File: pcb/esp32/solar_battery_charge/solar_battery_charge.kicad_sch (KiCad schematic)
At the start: 15 parts, among them J1 USB_A, J2 capacitor2, J3 Conn_01x02_Female, J4 Screw_Terminal_01x02, J5 Conn_01x02_Female, J6 Conn_01x02_Female, J7 capacitor1, U1 LM7805_TO220, U2 LM1117-5.0, U3 TP4056_complete_module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

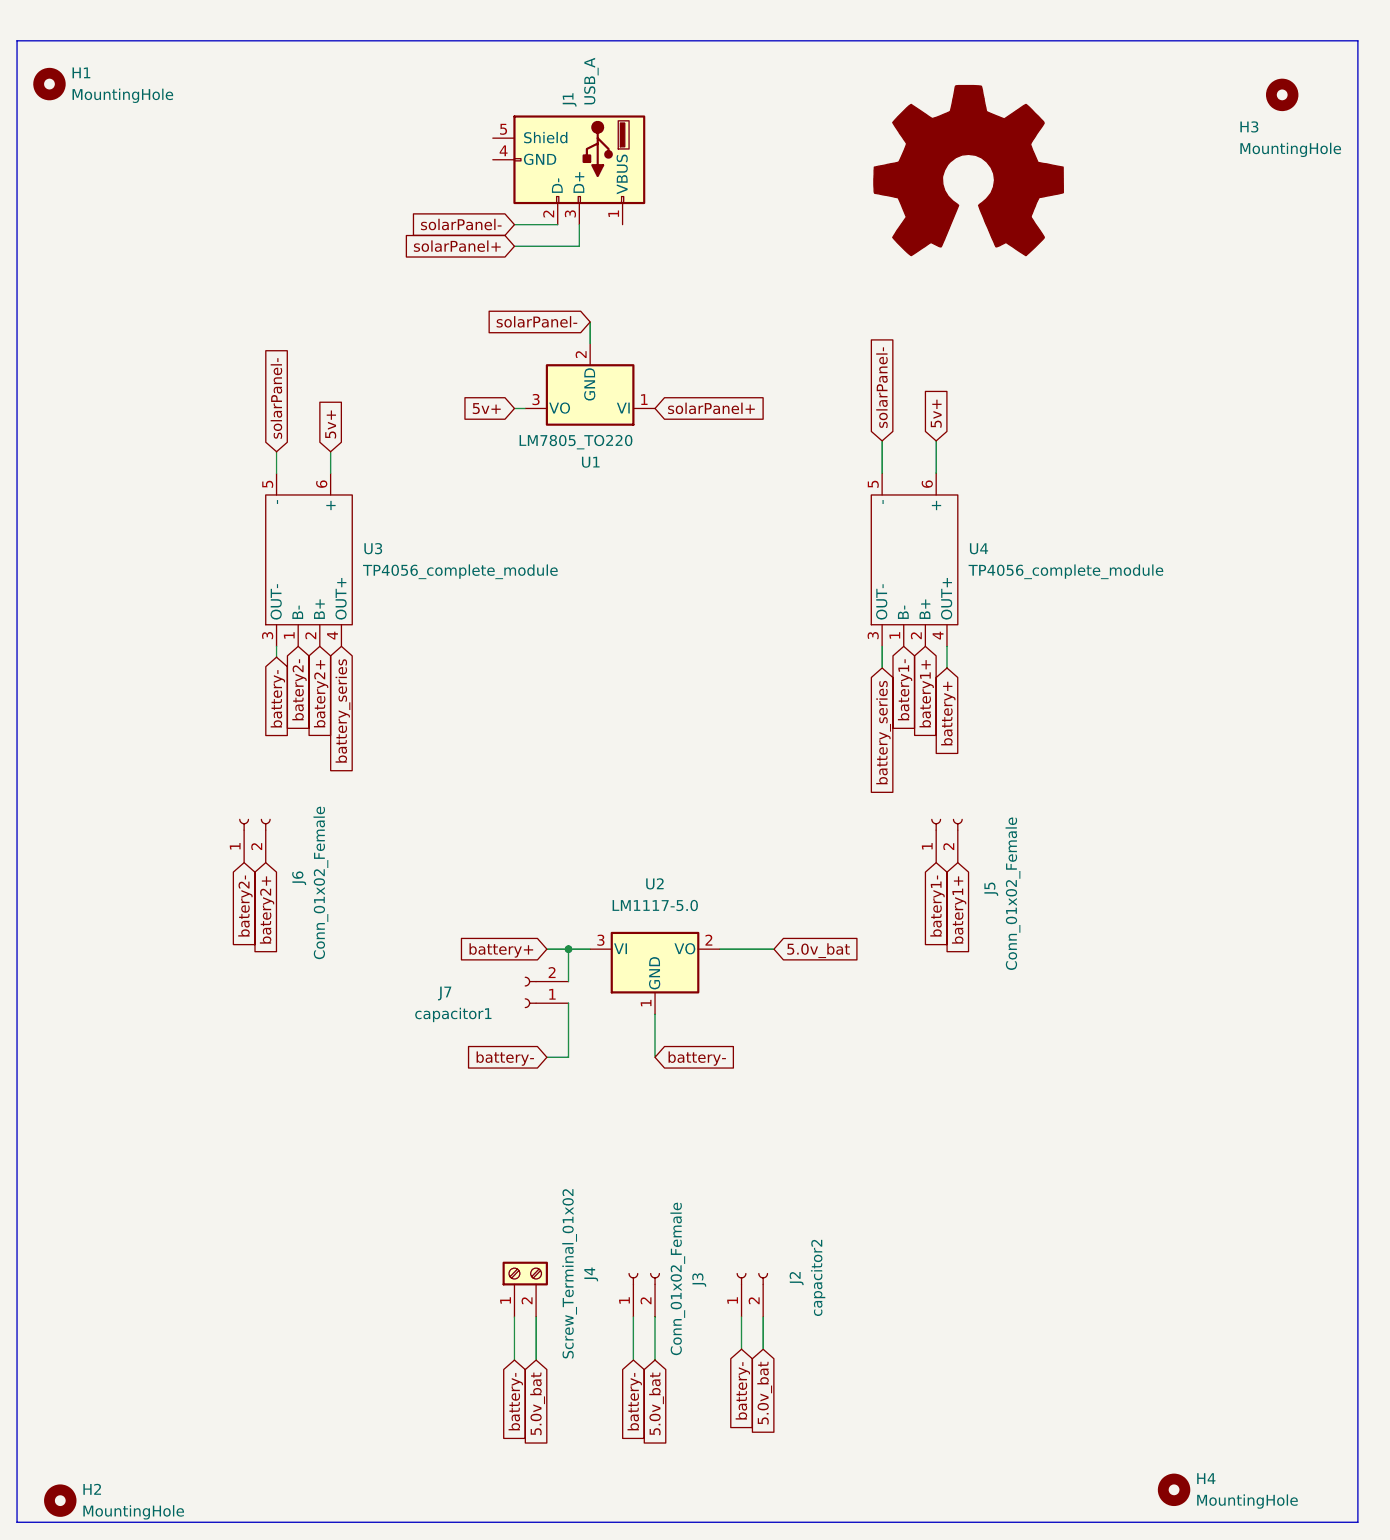
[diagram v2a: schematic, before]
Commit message: added 2 pairs of male pins to measure solar panel voltage and battery voltage
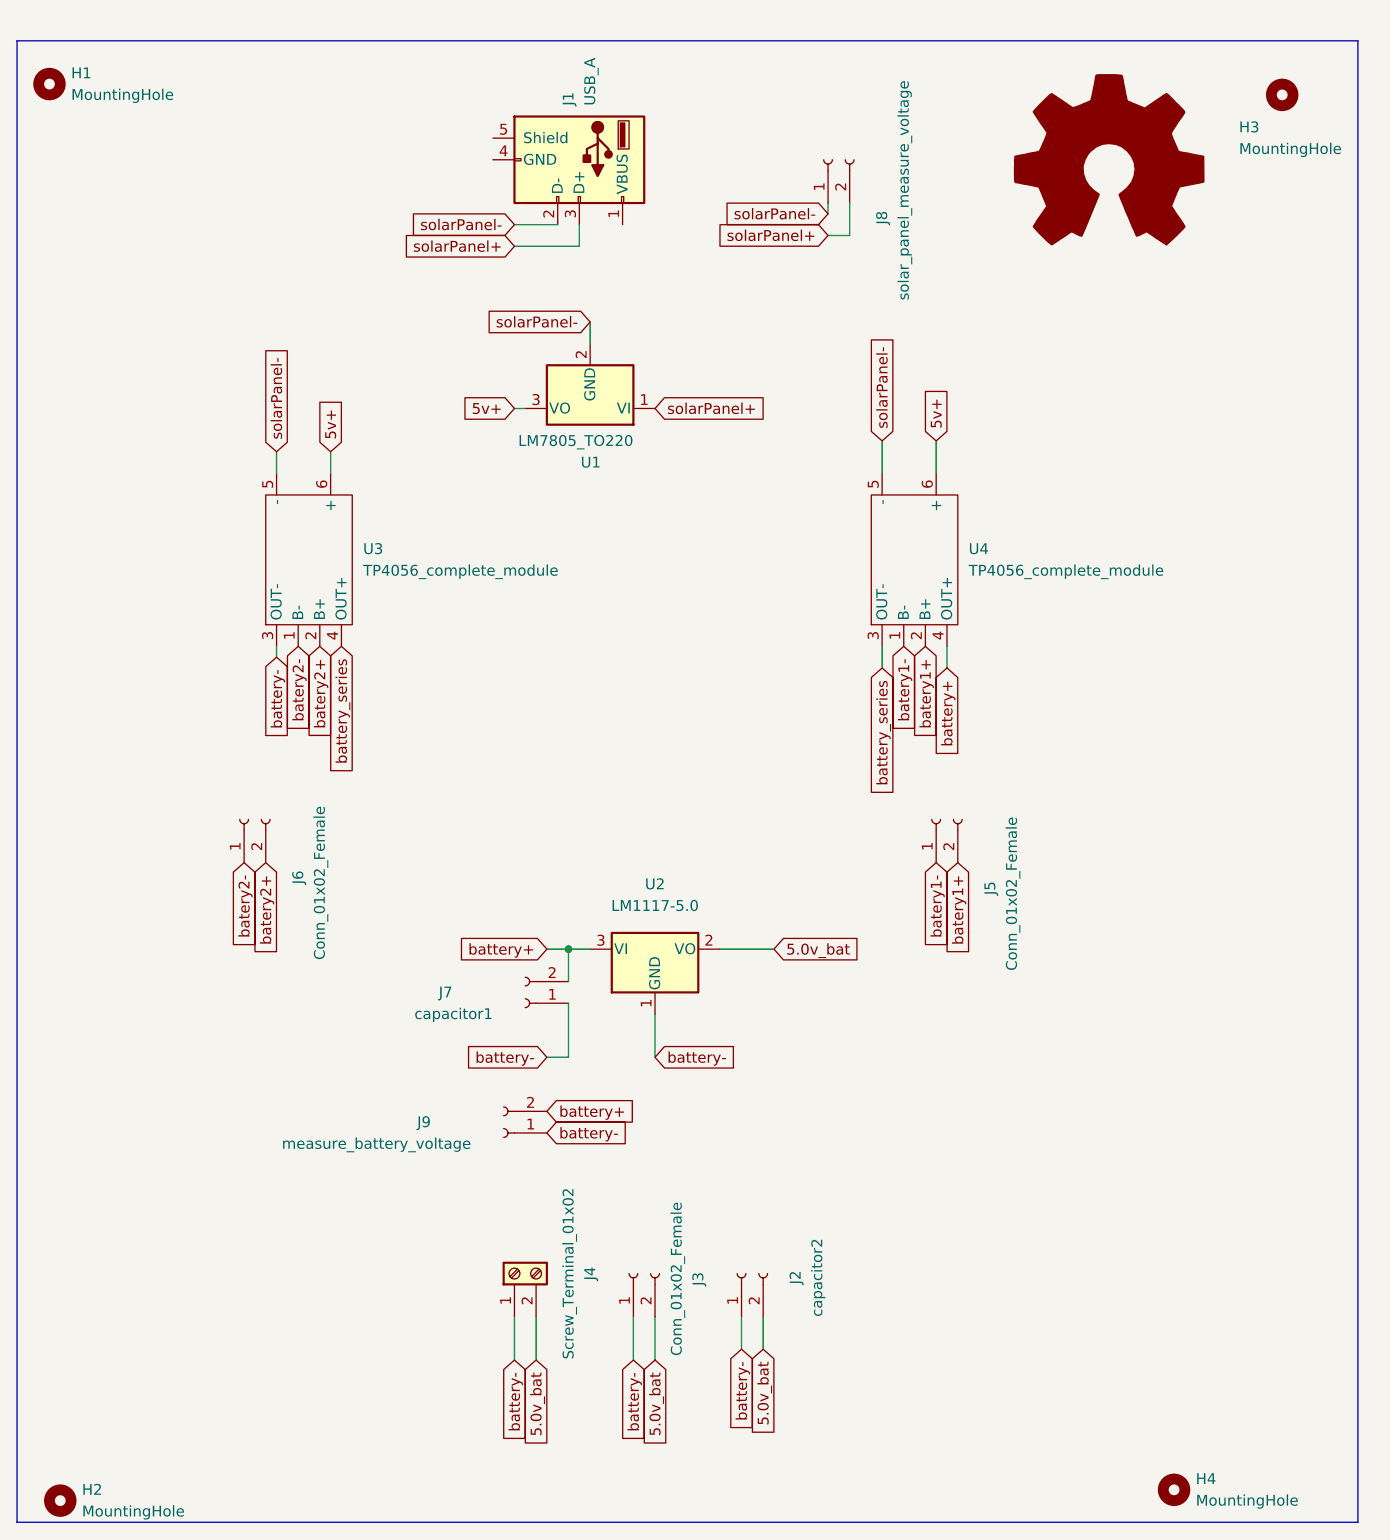
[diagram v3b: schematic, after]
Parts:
- added J8: solar_panel_measure_voltage, smart_sensor:Connector_Molex_Molex_SL_171971-0004_1x02_P2.54mm_Vertical_squares, symbol Connector:Conn_01x02_Female
- added J9: measure_battery_voltage, smart_sensor:Connector_Molex_Molex_SL_171971-0004_1x02_P2.54mm_Vertical_squares, symbol Connector:Conn_01x02_Female
- U2: footprint (none) -> Package_TO_SOT_SMD:SOT-223-3_TabPin2
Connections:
- net battery+: now also J9.2 (Pin_2)
- net battery-: now also J9.1 (Pin_1)
- net solarPanel+: now also J8.2 (Pin_2)
- net solarPanel-: now also J8.1 (Pin_1)
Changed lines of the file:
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@@
   (junction (at 80.01 121.92) (diameter 0) (color 0 0 0 0)
   )
+  (wire (pts (xy 113.03 34.29) (xy 113.03 38.1))
+    (stroke (width 0) (type default) (color 0 0 0 0))
+  )
   (wire (pts (xy 124.46 88.9) (xy 124.46 86.36))
     (stroke (width 0) (type default) (color 0 0 0 0))
@@
     (stroke (width 0) (type default) (color 0 0 0 0))
   )
+  (wire (pts (xy 113.03 38.1) (xy 110.49 38.1))
+    (stroke (width 0) (type default) (color 0 0 0 0))
+  )
   (wire (pts (xy 80.01 128.27) (xy 80.01 134.62))
     (stroke (width 0) (type default) (color 0 0 0 0))
@@
     (stroke (width 0) (type default) (color 0 0 0 0))
   )
+  (wire (pts (xy 110.49 34.29) (xy 110.49 35.56))
+    (stroke (width 0) (type default) (color 0 0 0 0))
+  )
   (wire (pts (xy 90.17 165.1) (xy 90.17 170.18))
     (stroke (width 0) (type default) (color 0 0 0 0))
@@
     )
   )
+  (global_label "solarPanel+" (shape input) (at 110.49 38.1 180) (fields_autoplaced)
+    (effects (font (size 1.27 1.27)) (justify right))
+    (property "Intersheet References" "${INTERSHEET_REFS}" (id 0) (at 96.405 38.1794 0)
+      (effects (font (size 1.27 1.27)) (justify right) hide)
+    )
+  )
   (global_label "battery+" (shape input) (at 124.46 88.9 270) (fields_autoplaced)
     (effects (font (size 1.27 1.27)) (justify right))
@@
     )
   )
+  (global_label "solarPanel-" (shape input) (at 110.49 35.56 180) (fields_autoplaced)
+    (effects (font (size 1.27 1.27)) (justify right))
+    (property "Intersheet References" "${INTERSHEET_REFS}" (id 0) (at 96.405 35.6394 0)
+      (effects (font (size 1.27 1.27)) (justify right) hide)
+    )
+  )
   (global_label "battery-" (shape input) (at 90.17 134.62 0) (fields_autoplaced)
     (effects (font (size 1.27 1.27)) (justify left))
@@
     )
   )
+  (global_label "battery-" (shape input) (at 77.47 143.51 0) (fields_autoplaced)
+    (effects (font (size 1.27 1.27)) (justify left))
+    (property "Intersheet References" "${INTERSHEET_REFS}" (id 0) (at 88.0474 143.4306 0)
+      (effects (font (size 1.27 1.27)) (justify left) hide)
+    )
+  )
+  (global_label "battery+" (shape input) (at 77.47 140.97 0) (fields_autoplaced)
+    (effects (font (size 1.27 1.27)) (justify left))
+    (property "Intersheet References" "${INTERSHEET_REFS}" (id 0) (at 88.0474 140.8906 0)
+      (effects (font (size 1.27 1.27)) (justify left) hide)
+    )
+  )
   (global_label "5.0v_bat" (shape input) (at 90.17 170.18 270) (fields_autoplaced)
     (effects (font (size 1.27 1.27)) (justify right))
@@
     )
   )
-  (symbol (lib_id "Graphic:Logo_Open_Hardware_Large") (at 127 31.75 0) (unit 1)
-    (in_bom yes) (on_board yes) (fields_autoplaced)
-    (property "Reference" "#LOGO1" (id 0) (at 127 19.05 0)
-      (effects (font (size 1.27 1.27)) hide)
-    )
-    (property "Value" "Logo_Open_Hardware_Large" (id 1) (at 127 41.91 0)
-      (effects (font (size 1.27 1.27)) hide)
-    )
-    (property "Footprint" "" (id 2) (at 127 31.75 0)
-      (effects (font (size 1.27 1.27)) hide)
-    )
-    (property "Datasheet" "~" (id 3) (at 127 31.75 0)
+  (symbol (lib_id "Graphic:Logo_Open_Hardware_Large") (at 143.51 30.48 0) (unit 1)
+    (in_bom yes) (on_board yes) (fields_autoplaced)
+    (property "Reference" "#LOGO1" (id 0) (at 143.51 17.78 0)
+      (effects (font (size 1.27 1.27)) hide)
+    )
+    (property "Value" "Logo_Open_Hardware_Large" (id 1) (at 143.51 40.64 0)
+      (effects (font (size 1.27 1.27)) hide)
+    )
+    (property "Footprint" "" (id 2) (at 143.51 30.48 0)
+      (effects (font (size 1.27 1.27)) hide)
+    )
+    (property "Datasheet" "~" (id 3) (at 143.51 30.48 0)
       (effects (font (size 1.27 1.27)) hide)
     )
@@
     )
   )
+  (symbol (lib_id "Connector:Conn_01x02_Female") (at 110.49 29.21 90) (unit 1)
+    (in_bom yes) (on_board yes)
+    (property "Reference" "J8" (id 0) (at 116.84 36.83 0)
+      (effects (font (size 1.27 1.27)) (justify left))
+    )
+    (property "Value" "solar_panel_measure_voltage" (id 1) (at 119.38 45.72 0)
+      (effects (font (size 1.27 1.27)) (justify left))
+    )
+    (property "Footprint" "smart_sensor:Connector_Molex_Molex_SL_171971-0004_1x02_P2.54mm_Vertical_squares" (id 2) (at 110.49 29.21 0)
+      (effects (font (size 1.27 1.27)) hide)
+    )
+    (property "Datasheet" "~" (id 3) (at 110.49 29.21 0)
+      (effects (font (size 1.27 1.27)) hide)
+    )
+    (pin "1")
+    (pin "2")
+  )
   (symbol (lib_id "Connector:Conn_01x02_Female") (at 87.63 160.02 90) (unit 1)
     (in_bom yes) (on_board yes) (fields_autoplaced)
@@
     (pin "2")
   )
+  (symbol (lib_id "Connector:Conn_01x02_Female") (at 72.39 143.51 180) (unit 1)
+    (in_bom yes) (on_board yes)
+    (property "Reference" "J9" (id 0) (at 62.23 142.24 0)
+      (effects (font (size 1.27 1.27)) (justify right))
+    )
+    (property "Value" "measure_battery_voltage" (id 1) (at 68.58 144.78 0)
+      (effects (font (size 1.27 1.27)) (justify left))
+    )
+    (property "Footprint" "smart_sensor:Connector_Molex_Molex_SL_171971-0004_1x02_P2.54mm_Vertical_squares" (id 2) (at 72.39 143.51 0)
+      (effects (font (size 1.27 1.27)) hide)
+    )
+    (property "Datasheet" "~" (id 3) (at 72.39 143.51 0)
+      (effects (font (size 1.27 1.27)) hide)
+    )
+    (pin "1")
+    (pin "2")
+  )
   (symbol (lib_id "Regulator_Linear:LM7805_TO220") (at 82.55 58.42 180) (unit 1)
     (in_bom yes) (on_board yes)
@@
     (property "Reference" "U2" (id 0) (at 90.17 114.3 0))
     (property "Value" "LM1117-5.0" (id 1) (at 90.17 116.84 0))
-    (property "Footprint" "" (id 2) (at 90.17 121.92 0)
+    (property "Footprint" "Package_TO_SOT_SMD:SOT-223-3_TabPin2" (id 2) (at 90.17 121.92 0)
       (effects (font (size 1.27 1.27)) hide)
     )
@@
       (reference "J7") (unit 1) (value "capacitor1") (footprint "smart_sensor:Connector_Molex_Molex_SL_171971-0004_1x02_P2.54mm_Vertical_squares")
     )
+    (path "/722b15d7-78ed-4a9a-8219-3b1ca0fe2723"
+      (reference "J8") (unit 1) (value "solar_panel_measure_voltage") (footprint "smart_sensor:Connector_Molex_Molex_SL_171971-0004_1x02_P2.54mm_Vertical_squares")
+    )
+    (path "/b54b557d-28f9-4508-a26a-2b658edac437"
+      (reference "J9") (unit 1) (value "measure_battery_voltage") (footprint "smart_sensor:Connector_Molex_Molex_SL_171971-0004_1x02_P2.54mm_Vertical_squares")
+    )
     (path "/c36a9a9a-1d9e-4ab6-a67f-0c9f31ad7ce6"

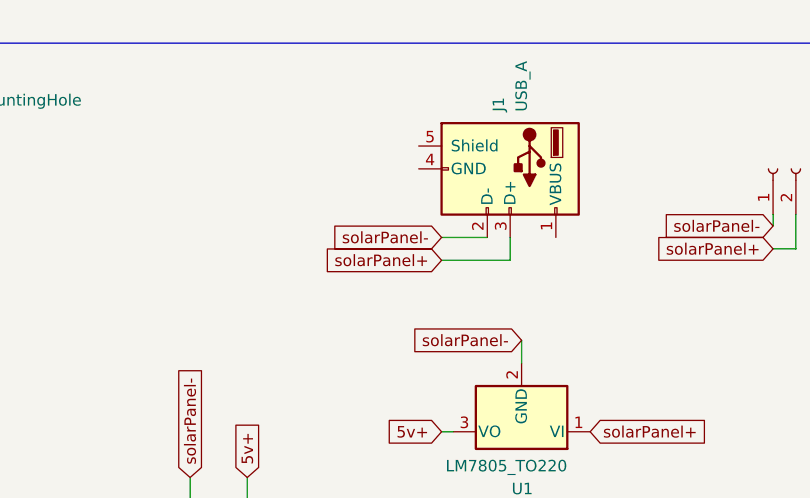
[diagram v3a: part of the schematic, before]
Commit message: added new pins to connect more 3.3v sensors and 5.0v sensors, also added 2 pull up resistors for sda and scl pins
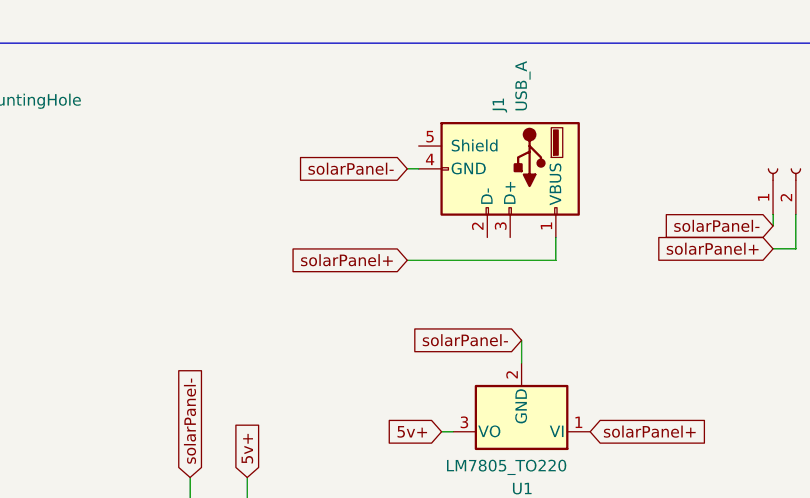
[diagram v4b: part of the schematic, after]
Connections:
- net solarPanel+: now also J1.1 (VBUS); no longer J1.3 (D+)
- net solarPanel-: now also J1.4 (GND); no longer J1.2 (D-)
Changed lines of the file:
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@@
+    (stroke (width 0) (type default) (color 0 0 0 0))
+  )
+  (wire (pts (xy 69.85 29.21) (xy 71.12 29.21))
+    (stroke (width 0) (type default) (color 0 0 0 0))
+  )
+  (wire (pts (xy 86.36 39.37) (xy 86.36 36.83))
+    (stroke (width 0) (type default) (color 0 0 0 0))
+  )
+  (wire (pts (xy 69.85 39.37) (xy 86.36 39.37))
     (stroke (width 0) (type default) (color 0 0 0 0))
   )
@@
     (stroke (width 0) (type default) (color 0 0 0 0))
   )
-  (wire (pts (xy 81.28 39.37) (xy 81.28 36.83))
-    (stroke (width 0) (type default) (color 0 0 0 0))
-  )
-  (wire (pts (xy 73.66 36.83) (xy 78.74 36.83))
-    (stroke (width 0) (type default) (color 0 0 0 0))
-  )
   (wire (pts (xy 113.03 38.1) (xy 110.49 38.1))
     (stroke (width 0) (type default) (color 0 0 0 0))
@@
     (stroke (width 0) (type default) (color 0 0 0 0))
   )
-  (wire (pts (xy 73.66 39.37) (xy 81.28 39.37))
-    (stroke (width 0) (type default) (color 0 0 0 0))
-  )
   (wire (pts (xy 73.66 165.1) (xy 73.66 170.18))
     (stroke (width 0) (type default) (color 0 0 0 0))
@@
     )
   )
-  (global_label "solarPanel+" (shape input) (at 73.66 39.37 180) (fields_autoplaced)
-    (effects (font (size 1.27 1.27)) (justify right))
-    (property "Intersheet References" "${INTERSHEET_REFS}" (id 0) (at 59.575 39.4494 0)
+  (global_label "solarPanel+" (shape input) (at 69.85 39.37 180) (fields_autoplaced)
+    (effects (font (size 1.27 1.27)) (justify right))
+    (property "Intersheet References" "${INTERSHEET_REFS}" (id 0) (at 55.765 39.4494 0)
       (effects (font (size 1.27 1.27)) (justify right) hide)
     )
@@
     )
   )
-  (global_label "solarPanel-" (shape input) (at 73.66 36.83 180) (fields_autoplaced)
-    (effects (font (size 1.27 1.27)) (justify right))
-    (property "Intersheet References" "${INTERSHEET_REFS}" (id 0) (at 59.575 36.9094 0)
-      (effects (font (size 1.27 1.27)) (justify right) hide)
-    )
+  (global_label "solarPanel-" (shape input) (at 69.85 29.21 180) (fields_autoplaced)
+    (effects (font (size 1.27 1.27)) (justify right))
+    (property "Intersheet References" "${INTERSHEET_REFS}" (id 0) (at 55.765 29.2894 0)
+      (effects (font (size 1.27 1.27)) (justify right) hide)
+    )
